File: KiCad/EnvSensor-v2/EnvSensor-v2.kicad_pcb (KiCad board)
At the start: 2 copper layers, 120 x 100 mm, 155 parts, among them J1 Conn_01x06, J10 Conn_01x02, J2 Conn_01x02, J3 USB_B_Micro, J4 Conn_01x02, J5 Micro_SD_Card_Det, J6 Conn_01x02, J8 HPMA115C0-003, J9 Conn_01x02, P1 USB_C_Plug_USB2.0, Q1 IRLML2502, Q2 Si3407DV, Q3 AUiRLR3110Z, Q4 AO6804A, SW1 SW_Push, SW2 Reset, SW3 SW_Push, SW4 SW_Push, SW5 SW_Push, U1 STM32L451RETx, U10 LTC3440, U11 MCP1826S-5.0, U12 MCP1825S-3.3, U2 E-Ink_Waveshare_4.2, U3 SCD30, U4 SCD40, U5 BME280, U6 AP9101CK, U7 MCP73843-4.2, U8 BME280-Module, U9 LM2735XMF, Y1 16Hz, Y2 32768/12.5pF

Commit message: Work on pcb v2
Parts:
- added C44: 22u, Capacitor_SMD:C_1206_3216Metric, F.Cu at (122.9, 111.7)
- added C45: 1u, Capacitor_SMD:C_0805_2012Metric, F.Cu at (112.1, 84.9)
- added C46: 10u, Capacitor_SMD:C_0805_2012Metric, F.Cu at (108.4, 110.0)
- C20, C21, U5: moved to B.Cu
- J1: value Conn_01x06 -> JTAG; footprint Connector_PinHeader_2.54mm:PinHeader_1x06_P2.54mm_Horizontal -> Connector_PinHeader_2.54mm:PinHeader_1x06_P2.54mm_Vertical
- J8: footprint Connector_PinHeader_2.54mm:PinHeader_1x04_P2.54mm_Horizontal -> Connector_PinHeader_2.54mm:PinHeader_1x04_P2.54mm_Vertical
- JP4: footprint Jumper:SolderJumper-2_P1.3mm_Open_RoundedPad1.0x1.5mm -> Jumper:SolderJumper-2_P1.3mm_Bridged_RoundedPad1.0x1.5mm
- U1: value STM32L451RETx -> STM32L451RCT6
- moved J8 80.6 mm to (94.8, 54.2), turned to 90 degrees
- moved J1 41.5 mm to (120.2, 54.2)
- moved R13 41.4 mm to (120.9, 92.8), turned to 90 degrees
- moved R12 41.2 mm to (122.8, 92.8), turned to 90 degrees
- moved R39 38.8 mm to (104.1, 108.9), turned to 90 degrees
- moved R37 34.4 mm to (105.0, 111.6), turned to 180 degrees
- moved R35 32.6 mm to (105.0, 113.6)
- moved C43 32.1 mm to (103.0, 117.8), turned to 0 degrees
- moved C28 31.9 mm to (80.5, 128.2), turned to 180 degrees
- moved C33 31.1 mm to (103.0, 115.8), turned to 0 degrees
- moved R36 30.5 mm to (106.0, 108.9), turned to 270 degrees
- moved TP4 29.2 mm to (100.2, 128.8)
- moved R18 28.6 mm to (112.1, 86.8), turned to 0 degrees
- moved J9 28.5 mm to (114.1, 106.6), turned to 180 degrees
- moved TP1 28.1 mm to (77.7, 129.9), turned to 0 degrees
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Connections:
- J9 pad 1: Net-(C37-Pad1) -> Net-(C44-Pad1)
- JP6 pad 1: Net-(C37-Pad1) -> Net-(C44-Pad1)
- SW2 pad 1: NRST -> GND
- SW2 pad 2: GND -> NRST
- U1 pad 10: Net-(U1-Pad10) -> LED_2
- U1 pad 11: Net-(U1-Pad11) -> LED_1
- U1 pad 16: Net-(U1-Pad16) -> HPMA_RX
- U1 pad 17: Net-(U1-Pad17) -> HPMA_TX
- U1 pad 21: Net-(U1-Pad21) -> SCK
- U1 pad 23: Net-(U1-Pad23) -> MOSI
- U1 pad 24: Net-(U1-Pad24) -> E_INK_SELECT
- U1 pad 25: Net-(U1-Pad25) -> E_INK_CD
- U1 pad 26: Net-(U1-Pad26) -> E_INK_RESET
- U1 pad 27: Net-(U1-Pad27) -> E_INK_BUSY
- U1 pad 28: Net-(U1-Pad28) -> POWER_5V_ENABLE
- U1 pad 33: Net-(U1-Pad33) -> SWITCH_1
- U1 pad 34: Net-(U1-Pad34) -> SWITCH_2
- U1 pad 35: Net-(U1-Pad35) -> SWITCH_3
- U1 pad 36: Net-(U1-Pad36) -> SWITCH_4
- U1 pad 37: Net-(U1-Pad37) -> SDIO_POWER_ENABLE
- U1 pad 38: Net-(U1-Pad38) -> SDIO_DETECT
- U1 pad 39: Net-(U1-Pad39) -> SDIO_DATA0
- U1 pad 40: Net-(U1-Pad40) -> SDIO_DATA1
- U1 pad 41: Net-(U1-Pad41) -> SCD30_READY
- U1 pad 42: Net-(U1-Pad42) -> SCL
- U1 pad 43: Net-(U1-Pad43) -> SDA
- U1 pad 51: Net-(U1-Pad51) -> SDIO_DATA2
- U1 pad 52: Net-(U1-Pad52) -> SDIO_DATA3
- U1 pad 53: Net-(U1-Pad53) -> SDIO_CLK
- U1 pad 54: Net-(U1-Pad54) -> SDIO_CMD
- U1 pad 57: Net-(U1-Pad57) -> BATTERY_MEASURE_ENABLE
- U1 pad 58: Net-(U1-Pad58) -> BATTERY_MEASURE_INPUT
- U1 pad 8: Net-(U1-Pad8) -> LED_4
- U1 pad 9: Net-(U1-Pad9) -> LED_3
- U12 pad 1: Net-(U12-Pad1) -> Net-(C37-Pad1)
- U12 pad 2: Net-(U12-Pad2) -> GND
- U12 pad 3: Net-(U12-Pad3) -> Net-(C44-Pad1)
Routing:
- net GND: track 8.55 -> 363.4 mm, vias 0 -> 102
- net +3V3: track 0.00 -> 308.7 mm, vias 0 -> 9
- net +BATT: track 11.8 -> 250.8 mm, vias 0 -> 12
- net NRST: track 0.00 -> 96.7 mm, vias 0 -> 4
- net LED_3: track 0.00 -> 91.0 mm, vias 0 -> 1
- net LED_1: track 0.00 -> 87.3 mm, vias 0 -> 1
- net SDA: track 0.00 -> 82.5 mm, vias 0 -> 3
- net LED_4: track 0.00 -> 80.8 mm, vias 0 -> 1
- net SCL: track 0.00 -> 79.8 mm
- net LED_2: track 0.00 -> 77.1 mm, vias 0 -> 1
- net +5V: track 0.00 -> 66.1 mm, vias 0 -> 4
- net SWITCH_4: track 0.00 -> 61.5 mm
- net SWITCH_3: track 0.00 -> 61.0 mm
- net SWITCH_1: track 0.00 -> 60.7 mm
- net SWDIO: track 0.00 -> 60.0 mm, vias 0 -> 1
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- added copper zone on B.Cu, net GND
- added copper zone on F.Cu, net GND
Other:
- net class Default: clearance 0.1 -> 0.12
- net class Power: clearance 0.1 -> 0.12
- net class Thick: clearance 0.1 -> 0.12
- rule trace_clearance: 0.1 -> 0.12

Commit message: Finishing touches
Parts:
- added J7: I2C, Connector_PinSocket_2.54mm:PinSocket_1x04_P2.54mm_Vertical, B.Cu at (138.8, 54.2)
- J4: moved to F.Cu
- moved C23 5.60 mm to (60.4, 115.8), turned to 180 degrees
- moved J2 5.56 mm to (141.6, 78.5)
- moved JP1 5.56 mm to (138.9, 77.3)
- moved D11 2.00 mm to (60.8, 119.2)
- moved JP2 0.40 mm to (88.4, 73.8)
- moved R32 0.20 mm to (102.4, 111.8)
- moved Y1 0.11 mm to (100.8, 70.4)
- moved R36 0.10 mm to (106.0, 109.0)
- moved R39 0.10 mm to (104.1, 109.0)
- turned J4 to 180 degrees
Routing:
- net SDA: track 82.5 -> 132.1 mm
- net SCL: track 79.8 -> 114.4 mm, vias 0 -> 1
- net +3V3: track 308.7 -> 323.1 mm
- net GND: track 363.4 -> 376.1 mm, vias 102 -> 104
- net Net-(R30-Pad2): track 26.9 -> 24.4 mm
- net Net-(C23-Pad1): track 30.0 -> 32.0 mm
- net VBUS: track 50.2 -> 52.0 mm
- net Net-(J2-Pad1): track 33.3 -> 34.1 mm
- net +BATT: track 250.8 -> 251.0 mm, vias 12 -> 44
- added copper zone on B.Cu, net +BATT
- added copper zone on F.Cu, net +BATT
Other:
- board text added: "3V3"
- board text added: "GND"
- board text added: "SCL"
- board text added: "SDA"
- board text added: "STM32L451RCT6"

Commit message: pcb finishing touches
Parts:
- added R40: 30k, Resistor_SMD:R_0805_2012Metric, F.Cu at (102.4, 108.8)
- D14: footprint Diode_SMD:D_SOD-323 -> Diode_SMD:D_SOD-323_HandSoldering
- J5: footprint Connector_Card:microSD_HC_Hirose_DM3BT-DSF-PEJS -> Connector_Card:microSD_HC_Hirose_DM3AT-SF-PEJM5
- R28: footprint Resistor_SMD:R_0805_2012Metric -> Resistor_SMD:R_0603_1608Metric
- R32: value 60k4 -> 30k
- R37: value 73k2 -> 47k
- moved R19 12.0 mm to (72.4, 64.6), turned to 90 degrees
- moved R20 11.6 mm to (74.2, 64.6), turned to 90 degrees
- moved R21 10.2 mm to (75.2, 75.6), turned to 270 degrees
- moved R23 10.2 mm to (73.4, 75.6), turned to 270 degrees
- moved R24 10.2 mm to (71.6, 75.6), turned to 270 degrees
- moved Q2 4.82 mm to (78.2, 70.8)
- moved R22 4.62 mm to (78.2, 67.4)
- moved C18 4.44 mm to (74.0, 68.8), turned to 90 degrees
- moved C19 3.65 mm to (72.4, 68.8), turned to 90 degrees
- moved JP7 1.00 mm to (93.2, 109.4)
- moved JP2 0.72 mm to (88.0, 73.2)
- moved C8 0.40 mm to (87.2, 76.2)
- moved C45 0.20 mm to (111.9, 84.9)
- moved JP3 0.20 mm to (135.6, 103.4)
- moved R17 0.20 mm to (111.9, 83.0)
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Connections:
- net Net-(C11-Pad1) renamed /VBAT
- net Net-(C18-Pad2) renamed /SD_3V3
- R32 pad 2: GND -> Net-(R32-Pad2)
- U1 pad 37: SDIO_POWER_ENABLE -> Net-(U1-Pad37)
- U1 pad 38: SDIO_DETECT -> Net-(U1-Pad38)
- U1 pad 61: Net-(U1-Pad61) -> SDIO_DETECT
- U1 pad 62: Net-(U1-Pad62) -> SDIO_POWER_ENABLE
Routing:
- net SDIO_DATA0: track 40.7 -> 52.1 mm
- net SDIO_DETECT: track 39.1 -> 48.2 mm
- net SDIO_DATA1: track 42.3 -> 50.6 mm
- net SDIO_POWER_ENABLE: track 34.4 -> 39.4 mm
- net GND: track 376.1 -> 380.2 mm, vias 104 -> 103
- net SDIO_DATA3: track 49.3 -> 46.4 mm
- net SDIO_DATA2: track 47.9 -> 45.5 mm
- net +BATT: track 251.0 -> 249.4 mm
- net +5V: track 66.1 -> 67.6 mm
- net +3V3: track 323.1 -> 324.5 mm
- net Net-(R32-Pad2): track 0.00 -> 1.12 mm
- net SDIO_CMD: track 48.6 -> 49.6 mm
- net Net-(C41-Pad1): track 8.95 -> 9.95 mm
- net NRST: track 96.7 -> 97.6 mm
- net Net-(J4-Pad2): track 19.2 -> 18.4 mm
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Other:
- board text added: "5V"
- board text added: "HPMA115C0-00x"
- board text added: "I2C"
- board text added: "JTAG"
- board text added: "NRST"
- board text added: "Rx"
- board text added: "SWCLK"
- board text added: "SWDIO"
- board text added: "SWO"
- board text added: "Tx"

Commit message: Finishing
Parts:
- added SW6: Start, Button_Switch_SMD:SW_SPST_CK_RS282G05A3, F.Cu at (61.0, 138.8)
- added U13: ESP-12S, JPComms:ESP-12S, F.Cu at (144.4, 60.6)
- moved C8 5.66 mm to (91.2, 80.2)
- moved Q4 3.94 mm to (72.0, 132.6)
- moved U6 1.90 mm to (68.2, 132.4)
- moved R27 1.90 mm to (68.2, 129.6)
- moved R13 1.39 mm to (120.2, 94.0)
- moved R12 1.34 mm to (122.2, 94.0)
- moved R26 1.28 mm to (65.4, 129.4)
- moved C22 0.60 mm to (65.4, 132.6), turned to 270 degrees
- moved J7 0.60 mm to (139.4, 54.2)
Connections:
- U1 pad 29: Net-(U1-Pad29) -> WIFI_RX
- U1 pad 30: Net-(U1-Pad30) -> WFI_TX
- U1 pad 44: Net-(U1-Pad44) -> WIFI_RESET
- U1 pad 45: Net-(U1-Pad45) -> WIFI_ENABLE
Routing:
- net WFI_TX: track 0.00 -> 79.0 mm, vias 0 -> 2
- net WIFI_RX: track 0.00 -> 76.8 mm, vias 0 -> 2
- net WIFI_RESET: track 0.00 -> 74.7 mm, vias 0 -> 2
- net WIFI_ENABLE: track 0.00 -> 71.5 mm, vias 0 -> 2
- net GND: track 380.2 -> 440.5 mm, vias 103 -> 108
- net +3V3: track 324.5 -> 353.6 mm
- net SDA: track 132.1 -> 119.1 mm, vias 3 -> 2
- net Net-(Q4-Pad4): track 2.09 -> 7.54 mm, vias 0 -> 2
- net +BATT: track 249.4 -> 244.0 mm
- net LED_1: track 87.6 -> 83.9 mm
- net LED_4: track 81.1 -> 77.4 mm
- net LED_3: track 91.3 -> 87.6 mm
- net LED_2: track 77.3 -> 73.7 mm
- net SDIO_CMD: track 49.6 -> 46.1 mm
- net -BATT: track 69.0 -> 71.3 mm
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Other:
- board text added: "Environmental Sensors, v2 JP, 2021.11.19"
- board text added: "Start"

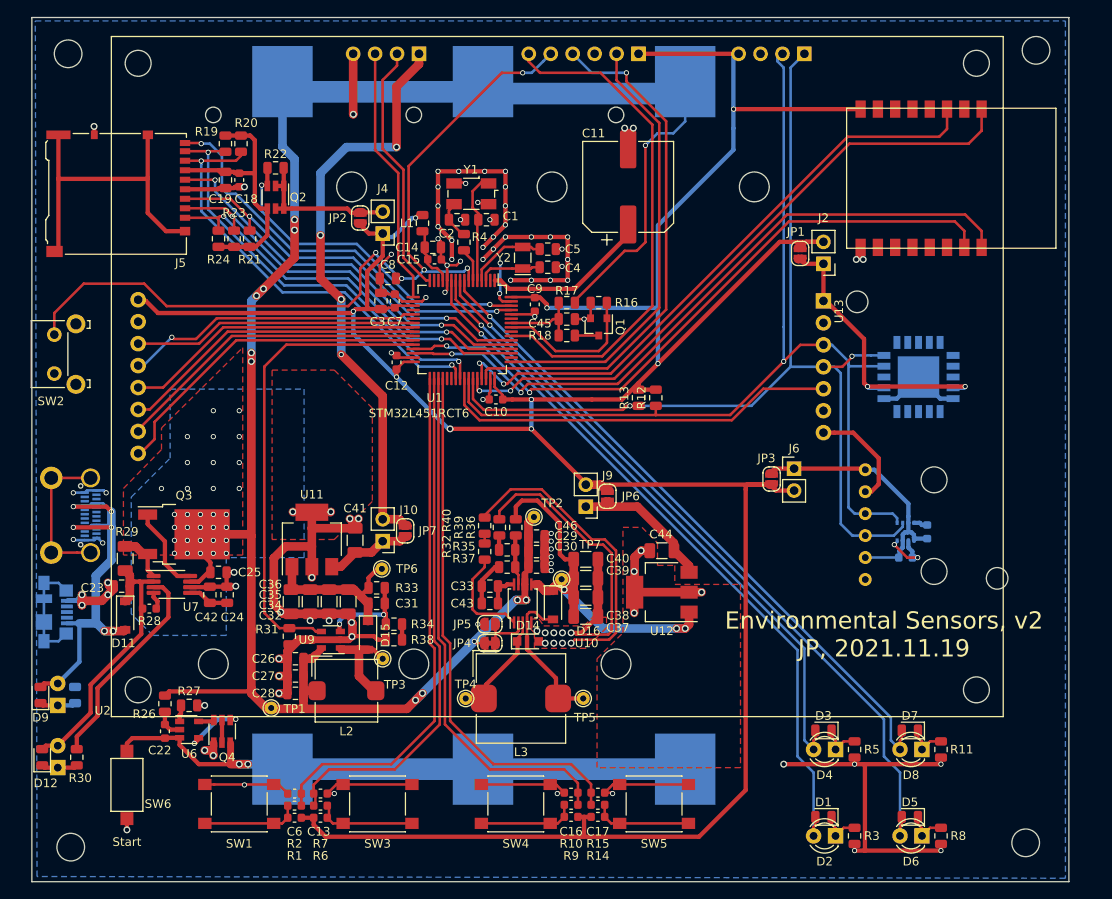
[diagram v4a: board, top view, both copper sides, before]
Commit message: Optimising ground pane
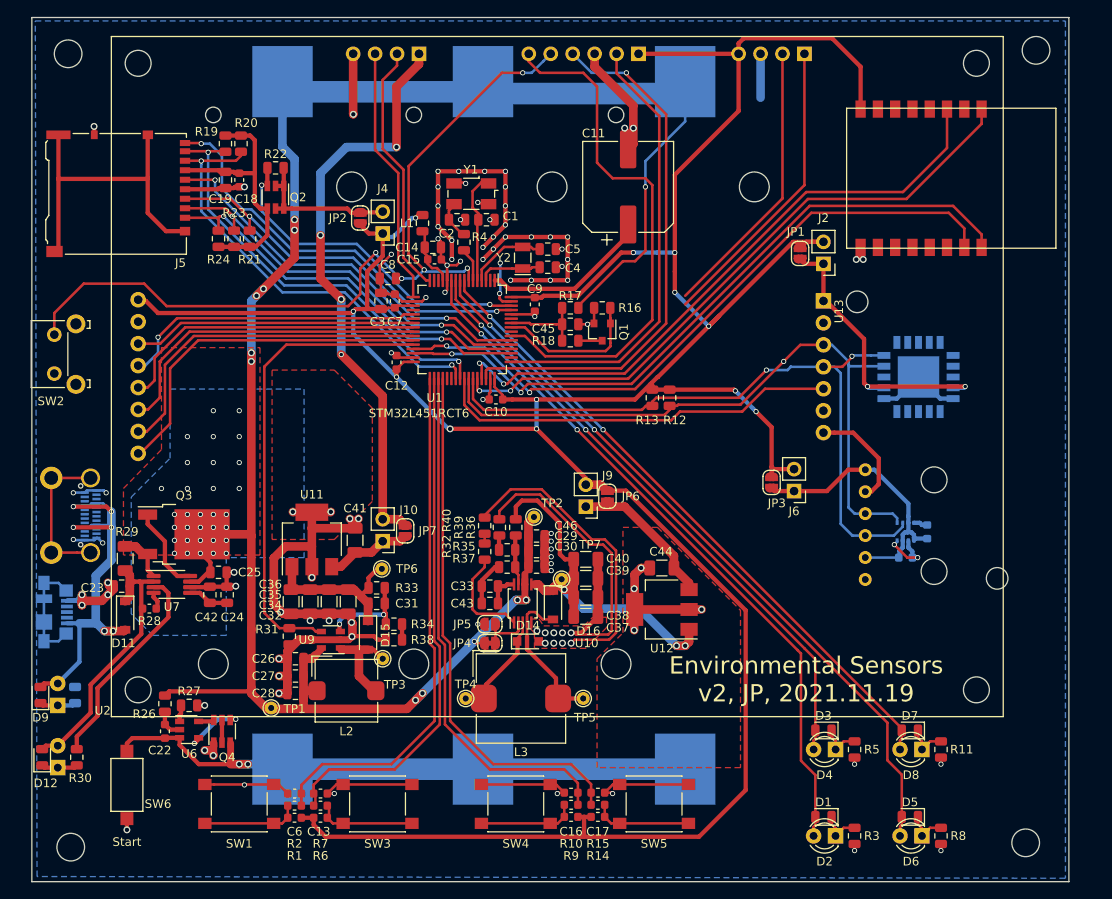
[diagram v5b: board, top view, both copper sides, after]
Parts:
- moved J6 2.60 mm to (138.2, 104.8), turned to 180 degrees
- moved C44 2.00 mm to (122.9, 113.7)
- moved U12 2.00 mm to (122.9, 118.5)
- moved R12 1.60 mm to (123.8, 94.0)
- moved R13 1.60 mm to (121.8, 94.0)
- moved Q1 0.72 mm to (116.0, 86.4)
- moved R18 0.72 mm to (112.3, 87.4)
- moved R16 0.72 mm to (116.0, 83.6)
- moved C45 0.72 mm to (112.3, 85.5)
- moved R17 0.72 mm to (112.3, 83.6)
- moved JP3 0.40 mm to (135.6, 103.8), turned to 90 degrees
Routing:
- net GND: track 440.5 -> 420.5 mm, vias 108 -> 107
- net +3V3: track 353.6 -> 366.7 mm, vias 9 -> 12
- net SCL: track 116.2 -> 112.1 mm
- net E_INK_RESET: track 36.9 -> 39.7 mm
- net SDA: track 119.1 -> 116.7 mm
- net LED_3: track 87.6 -> 85.5 mm, vias 1 -> 2
- net LED_2: track 73.7 -> 71.6 mm, vias 1 -> 2
- net LED_4: track 77.4 -> 75.3 mm, vias 1 -> 2
- net LED_1: track 83.9 -> 81.8 mm, vias 1 -> 2
- net E_INK_BUSY: track 38.9 -> 41.0 mm
- net SWO: track 58.9 -> 60.9 mm
- net E_INK_CD: track 36.1 -> 38.0 mm
- net WIFI_ENABLE: track 71.5 -> 72.8 mm
- net Net-(C44-Pad1): track 16.9 -> 18.0 mm
- net E_INK_SELECT: track 35.2 -> 36.2 mm
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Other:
- board text added: "Environmental Sensors v2, JP, 2021.11.19"
- board text removed: "Environmental Sensors, v2 JP, 2021.11.19"

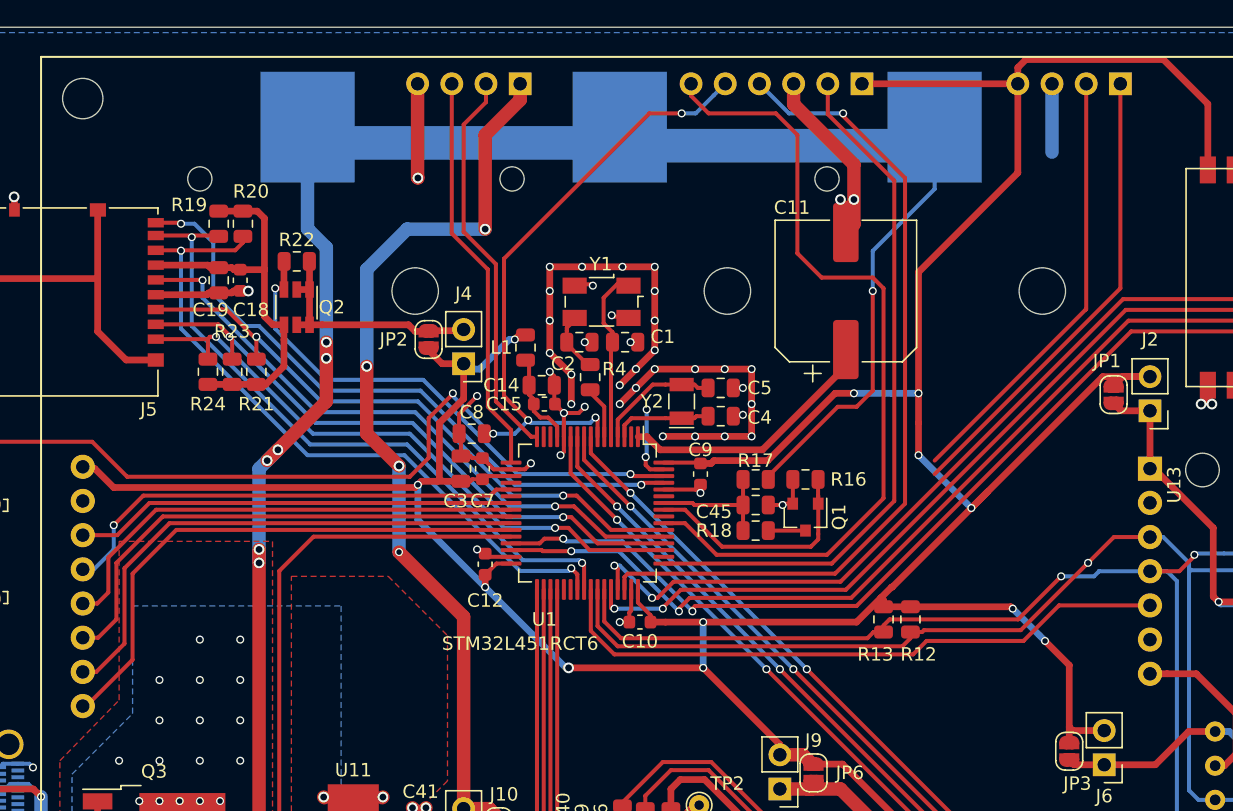
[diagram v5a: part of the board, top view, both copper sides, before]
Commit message: Optimising ground pane
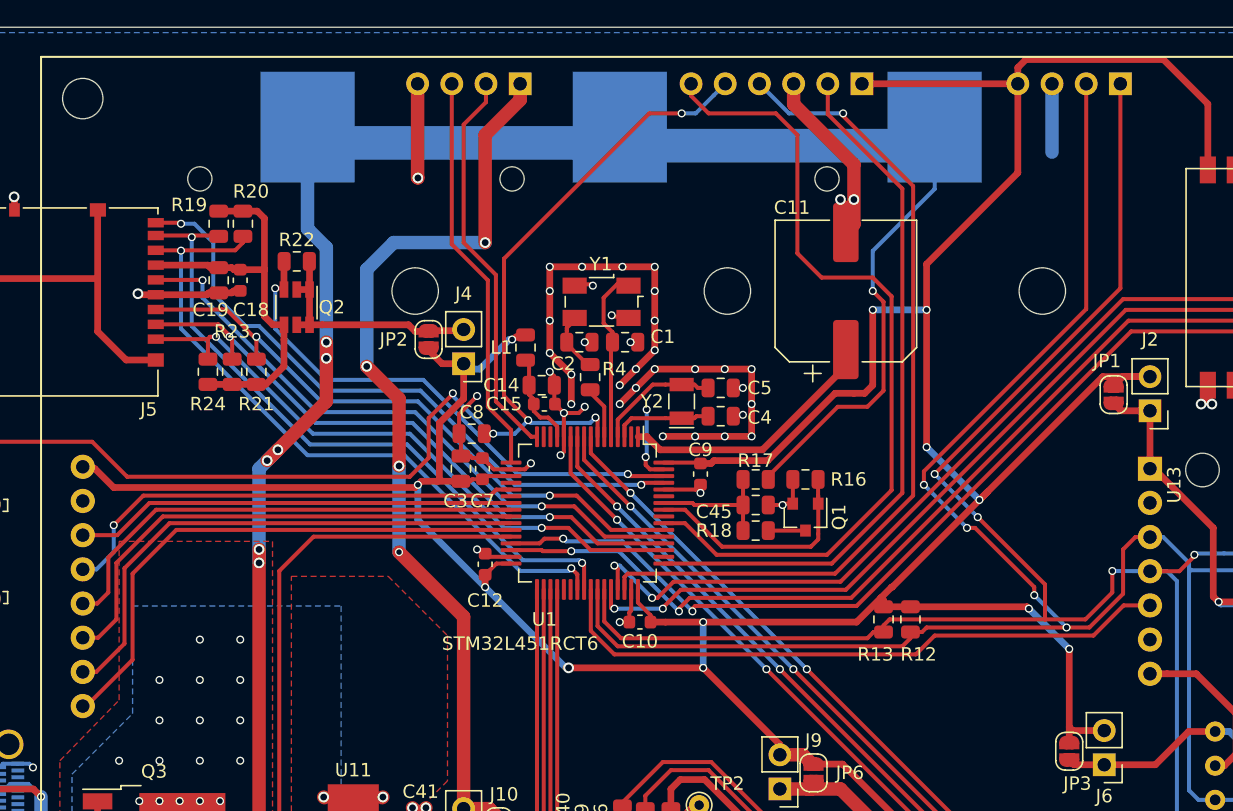
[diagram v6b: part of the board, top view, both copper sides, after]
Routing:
- net SCL: track 112.1 -> 131.5 mm, vias 1 -> 4
- net SDA: track 116.7 -> 131.8 mm, vias 2 -> 4
- net +3V3: track 366.7 -> 372.1 mm
- net +BATT: track 243.9 -> 245.1 mm
- net GND: track 420.5 -> 421.2 mm
- net +5V: track 67.8 -> 68.4 mm
